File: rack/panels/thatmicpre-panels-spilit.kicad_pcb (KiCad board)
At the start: 2 copper layers, 87.9 x 78 mm, 2 parts

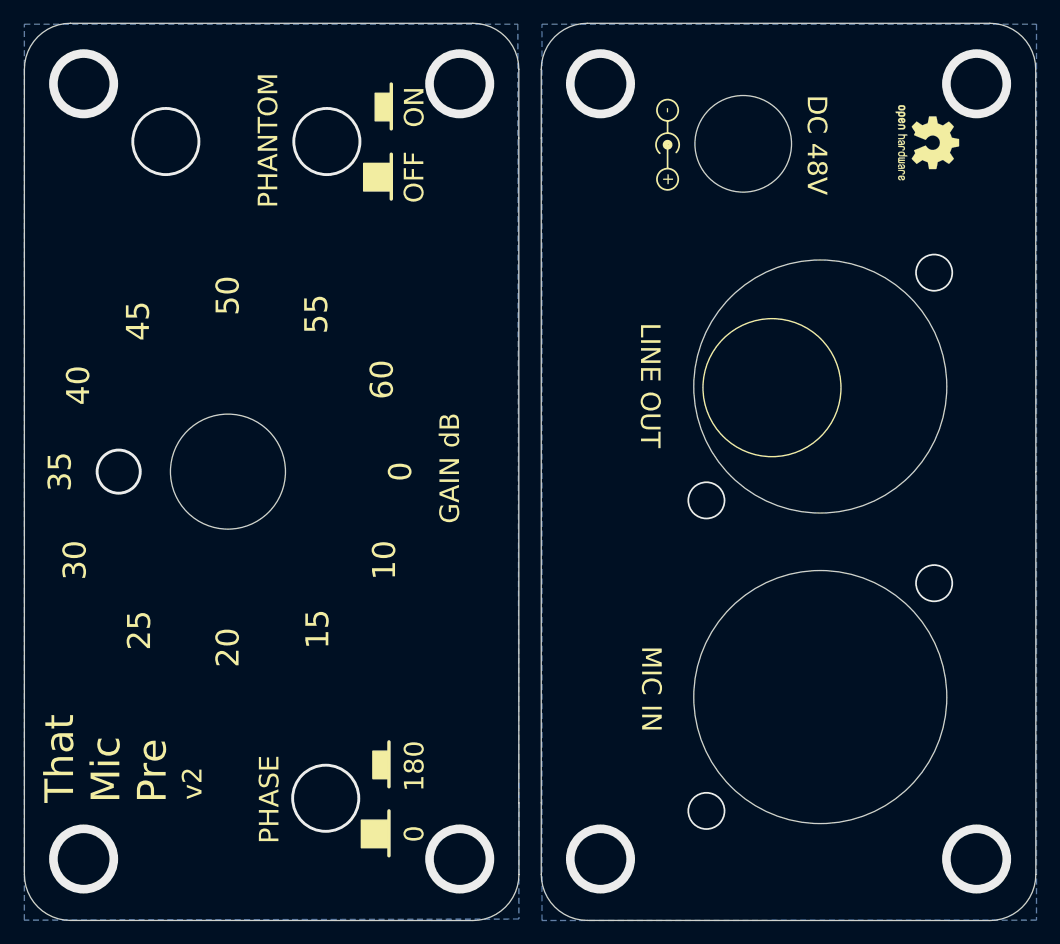
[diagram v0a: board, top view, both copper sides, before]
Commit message: Fix the bug where the hole positions and panel move in opposite directions, and optimize the size of the mounting holes
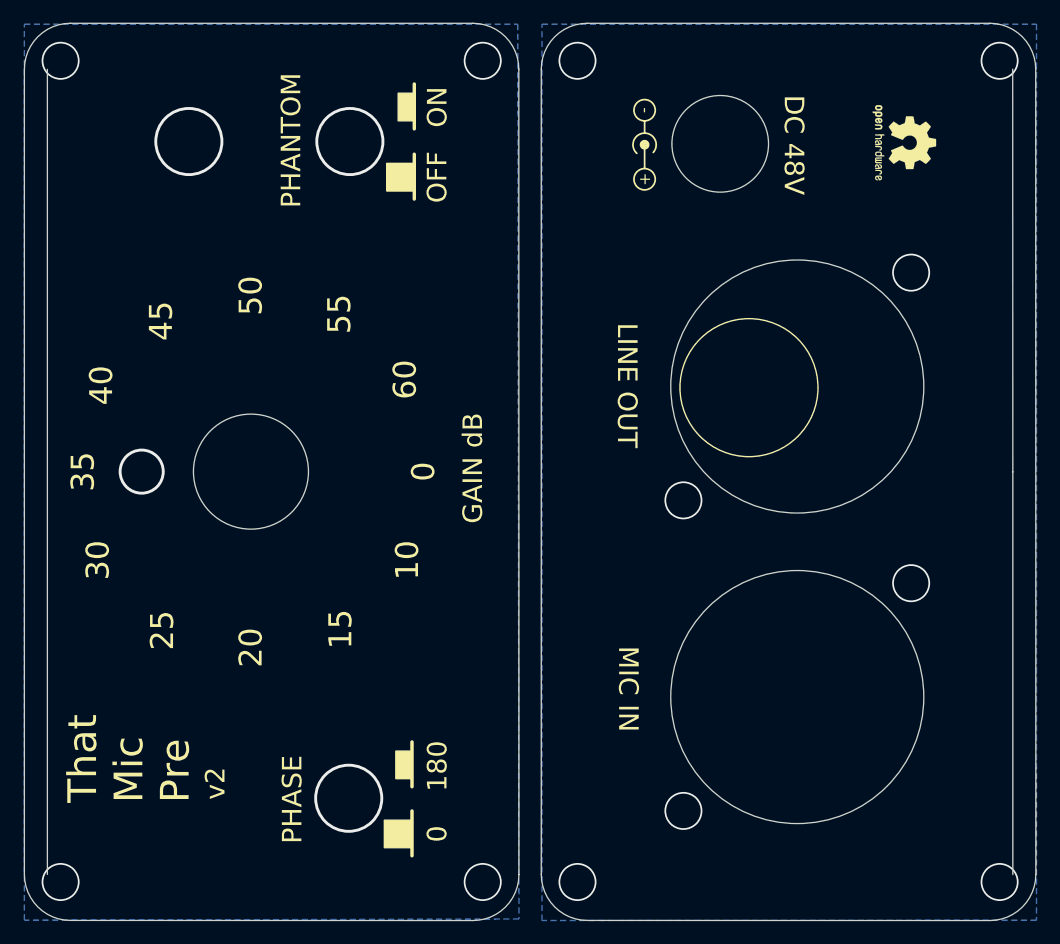
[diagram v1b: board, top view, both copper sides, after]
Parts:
- moved LOGO4 2.00 mm to (156.7, 65.0)
- moved REF** 2.00 mm to (179.2, 64.8)
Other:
- outline, holes or cut-outs redrawn

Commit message: Remove the unnecessary solid lines, and optimize the panel labels.
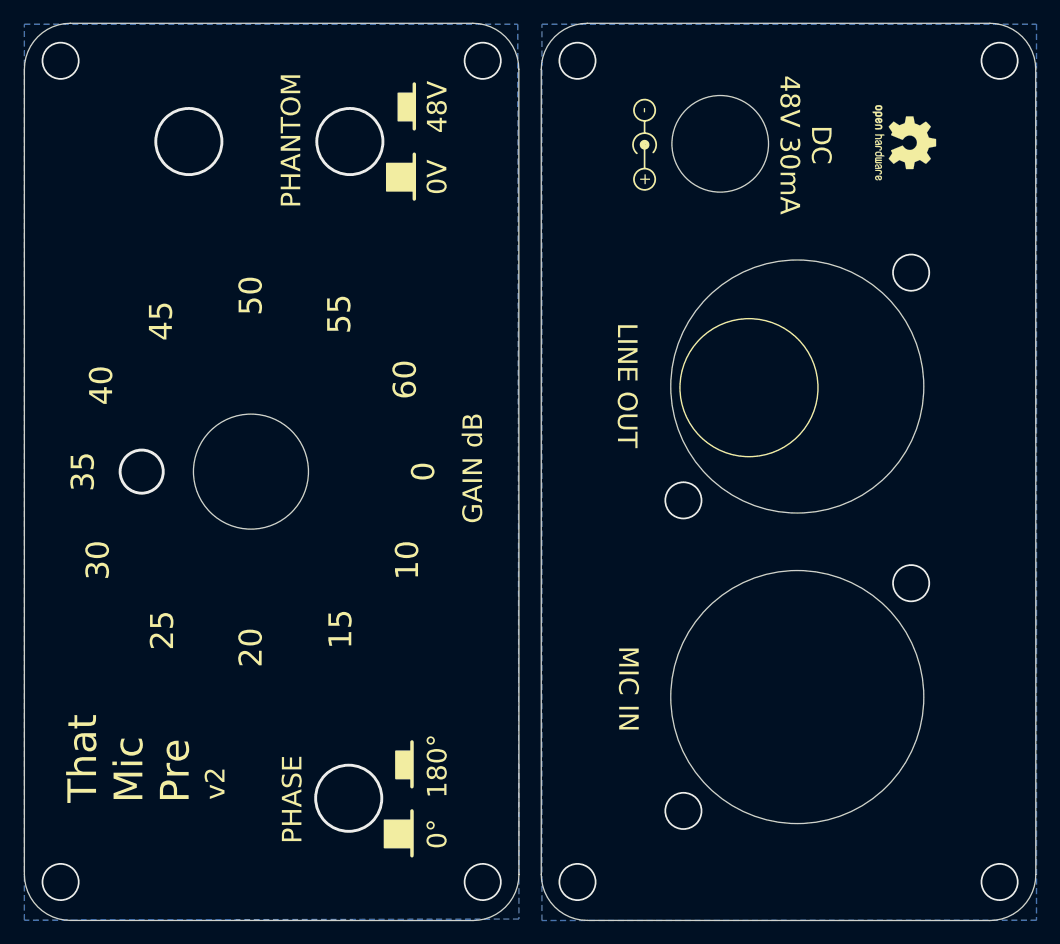
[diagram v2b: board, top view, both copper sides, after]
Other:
- outline, holes or cut-outs redrawn
- board text added: "0V"
- board text added: "0°"
- board text added: "180°"
- board text added: "48V"
- board text added: "DC 48V 30mA"
- board text removed: "180"
- board text removed: "DC 48V"
- board text removed: "OFF"
- board text removed: "ON"
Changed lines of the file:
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@@
-		(layer "Edge.Cuts")
-	)
-	(gr_line
-		(start 188.627984 93.411736)
-		(end 188.617984 58.405736)
-		(stroke
-			(width 0.05)
-			(type solid)
-		)
-		(layer "Edge.Cuts")
-	)
-	(gr_line
-		(start 188.627984 93.411736)
-		(end 188.627984 128.425736)
-		(stroke
-			(width 0.05)
-			(type solid)
-		)
 		(layer "Edge.Cuts")
 	)
@@
 		(layer "Edge.Cuts")
 	)
-	(gr_line
-		(start 104.687984 58.415736)
-		(end 104.687984 128.415736)
-		(stroke
-			(width 0.05)
-			(type solid)
-		)
-		(layer "Edge.Cuts")
-	)
 	(gr_circle
 		(center 163.187984 64.895736)
@@
 		)
 	)
-	(gr_text "DC 48V"
-		(at 169.587984 64.995736 -90)
+	(gr_text "DC \n48V 30mA"
+		(at 170.587984 64.995736 270)
 		(layer "F.SilkS")
 		(effects
@@
 		)
 	)
-	(gr_text "OFF"
+	(gr_text "0V"
 		(at 138.587984 67.795736 90)
 		(layer "F.SilkS")
@@
 		)
 	)
-	(gr_text "ON"
+	(gr_text "48V"
 		(at 138.6 61.7 90)
 		(layer "F.SilkS")
@@
 		)
 	)
-	(gr_text "0"
+	(gr_text "0°"
 		(at 138.587984 124.895736 90)
 		(layer "F.SilkS")
@@
 		)
 	)
-	(gr_text "180"
+	(gr_text "180°"
 		(at 138.6 119 90)
 		(layer "F.SilkS")
@@
 		(layer "F.Cu")
 		(pts
-			(xy 150.8 129) (xy 187.5 129)
+			(xy 150.8 135) (xy 187.5 135)
 		)
 		(height 20.9)
 		(gr_text "36.7000 mm"
-			(at 169.15 148.1 0)
+			(at 169.15 154.1 0)
 			(layer "F.Cu")
 			(effects
@@
 		(layer "F.Cu")
 		(pts
-			(xy 107.85 127) (xy 140.55 127.05)
+			(xy 49.631247 163.842159) (xy 82.331247 163.892159)
 		)
 		(height 23.051868)
 		(gr_text "32.7000 mm"
-			(at 124.167505 148.276843 359.9123918)
+			(at 65.948752 185.119002 359.9123918)
 			(layer "F.Cu")
 			(effects
@@
 		(layer "F.Cu")
 		(pts
-			(xy 107.9 59.5) (xy 107.9 126.9)
+			(xy 57.916 90.334) (xy 57.916 157.734)
 		)
 		(height 18.8)
 		(gr_text "67.4000 mm"
-			(at 87.3 93.2 90)
+			(at 37.316 124.034 90)
 			(layer "F.Cu")
 			(effects
@@
 		(layer "F.Cu")
 		(pts
-			(xy 187.5 57.6) (xy 187.5 129)
+			(xy 193.5 57.6) (xy 193.5 129)
 		)
 		(height -26.4)
 		(gr_text "71.4000 mm"
-			(at 212.1 93.3 90)
+			(at 218.1 93.3 90)
 			(layer "F.Cu")
 			(effects

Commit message: Fix the bug where the panel has a 1mm error(maked1 ). Move the hole of panels up by 1mm, and optimize the panel labels.
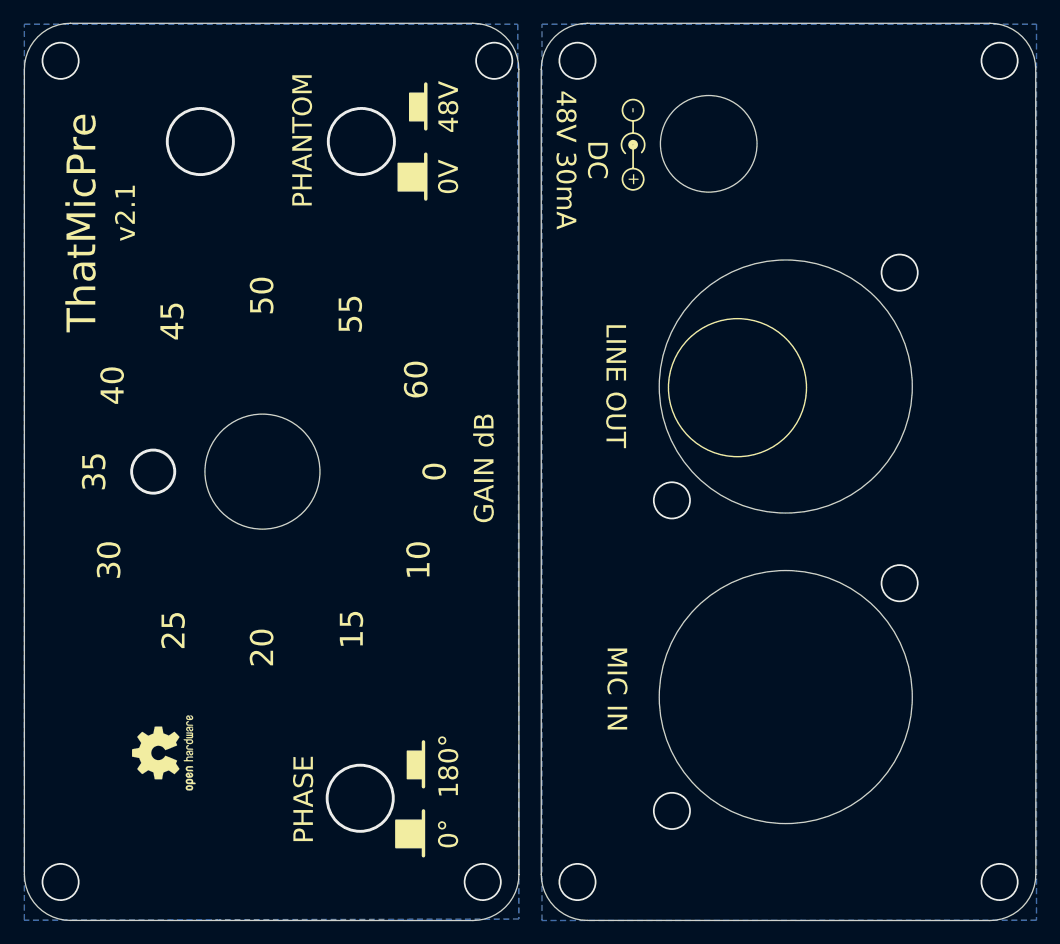
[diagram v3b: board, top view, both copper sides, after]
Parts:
- moved REF** 83.4 mm to (114.8, 117.9), turned to 90 degrees
- moved LOGO4 1.00 mm to (155.7, 65.0)
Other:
- outline, holes or cut-outs redrawn
- board text added: "ThatMicPre"
- board text added: "v2.1"
- board text removed: "That Mic Pre"
- board text removed: "v2"

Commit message: optimize the panel labels
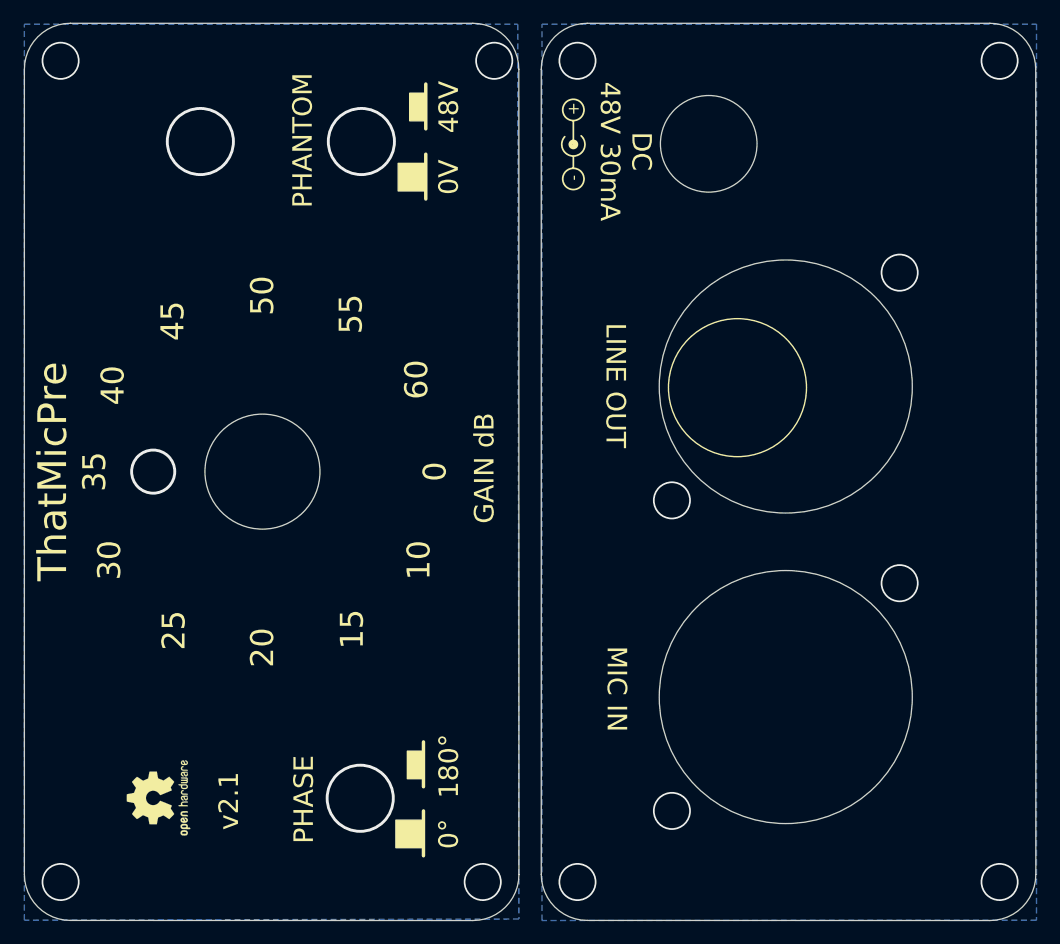
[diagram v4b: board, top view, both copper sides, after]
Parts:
- moved LOGO4 5.34 mm to (150.3, 64.9), turned to 90 degrees
- moved REF** 3.94 mm to (114.4, 121.8)
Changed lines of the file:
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@@
 	(footprint "Symbol:OSHW-Logo2_7.3x6mm_SilkScreen"
 		(layer "F.Cu")
-		(at 114.808 117.856 90)
+		(at 114.3508 121.7676 90)
 		(descr "Open Source Hardware Symbol")
 		(tags "Logo Symbol OSHW")
 		(property "Reference" "REF**"
-			(at 0 0 270)
+			(at 0 0 -90)
 			(layer "F.SilkS")
 			(hide yes)
@@
 		)
 		(property "Value" "OSHW-Logo2_7.3x6mm_SilkScreen"
-			(at 0.75 0 270)
+			(at 0.75 0 -90)
 			(layer "F.Fab")
 			(hide yes)
@@
 	(footprint "Symbol:Symbol_Barrel_Polarity"
 		(layer "F.Cu")
-		(at 155.687984 64.974736 -90)
+		(at 150.3438 64.9478 90)
 		(descr "Barrel connector polarity indicator")
 		(tags "barrel polarity")
 		(property "Reference" "LOGO4"
-			(at 0 -2 90)
+			(at 0 -2 270)
 			(layer "F.SilkS")
 			(hide yes)
@@
 		)
 		(property "Value" "SYM_Arrow_Normal"
-			(at 0 2 90)
+			(at 0 2 270)
 			(layer "F.Fab")
 			(hide yes)
@@
 		)
 		(property "Footprint" "Symbol:Symbol_Barrel_Polarity"
-			(at 0 0 -90)
+			(at 0 0 90)
 			(unlocked yes)
 			(layer "F.Fab")
@@
 		)
 		(property "Datasheet" ""
-			(at 0 0 -90)
+			(at 0 0 90)
 			(unlocked yes)
 			(layer "F.Fab")
@@
 		)
 		(property "Description" ""
-			(at 0 0 -90)
+			(at 0 0 90)
 			(unlocked yes)
 			(layer "F.Fab")
@@
 		(attr exclude_from_pos_files)
 		(fp_line
+			(start 0 0.075)
+			(end 2 0.075)
+			(stroke
+				(width 0.15)
+				(type solid)
+			)
+			(layer "F.SilkS")
+		)
+		(fp_line
 			(start -2 0.075)
 			(end -1.1 0.075)
-			(stroke
-				(width 0.15)
-				(type solid)
-			)
-			(layer "F.SilkS")
-		)
-		(fp_line
-			(start 0 0.075)
-			(end 2 0.075)
 			(stroke
 				(width 0.15)
@@
 		)
 		(fp_circle
-			(center -3 0.075)
-			(end -3 1)
+			(center 3 0.075)
+			(end 3 1)
 			(stroke
 				(width 0.15)
@@
 		)
 		(fp_circle
-			(center 3 0.075)
-			(end 3 1)
+			(center -3 0.075)
+			(end -3 1)
 			(stroke
 				(width 0.15)
@@
 	)
 	(gr_text "v2.1"
-		(at 111.506 70.866 90)
+		(at 120.4722 122.0216 90)
 		(layer "F.SilkS")
 		(effects
@@
 	)
 	(gr_text "+"
-		(at 155.687984 67.974736 -90)
+		(at 150.42 61.8462 90)
 		(layer "F.SilkS")
 		(effects
@@
 	)
 	(gr_text "DC \n48V 30mA"
-		(at 151.13 66.294 -90)
+		(at 154.9654 65.5574 -90)
 		(layer "F.SilkS")
 		(effects
@@
 	)
 	(gr_text "-"
-		(at 155.687984 61.974736 -90)
+		(at 150.42 67.8462 90)
 		(layer "F.SilkS")
 		(effects
@@
 	)
 	(gr_text "ThatMicPre"
-		(at 107.696 81.28 90)
-		(layer "F.SilkS")
-		(effects
+		(at 105.156 102.9208 90)
+		(layer "F.SilkS")
+		(effects
